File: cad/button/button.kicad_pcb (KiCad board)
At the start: 2 copper layers, 60 x 20 mm, 17 parts, among them J1 uSD_SPI, J2 SWD, SW1 SW_Push, U1 STM32L072KZTx, U2 PAM8302AAS

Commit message: more drawing
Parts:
- J1: footprint Connectors:microSD_Card_Receptacle_Wuerth_693072010801 -> custom:PJRC_uSD_Adapter; moved to B.Cu
- SW1: footprint Buttons_Switches_THT:SW_PUSH-12mm -> custom:SW_PUSH-12mm
- moved J2 57.4 mm to (52.8, 63.0), turned to 270 degrees
- moved BT1 47.5 mm to (29.0, 63.2), turned to 0 degrees
- moved R4 41.7 mm to (63.0, 46.0)
- moved LS1 39.4 mm to (66.9, 39.0), turned to 180 degrees
- moved U2 35.7 mm to (67.0, 46.0), turned to 90 degrees
- moved C2 33.0 mm to (27.0, 54.0), turned to 270 degrees
- moved C4 31.3 mm to (34.0, 58.0), turned to 0 degrees
- moved C1 30.7 mm to (27.0, 50.0), turned to 270 degrees
- moved U1 30.4 mm to (34.0, 51.0)
- moved SW1 30.2 mm to (46.5, 57.4)
- moved C5 27.1 mm to (27.0, 44.0), turned to 270 degrees
- moved R3 25.1 mm to (59.0, 55.0), turned to 180 degrees
- moved C6 24.8 mm to (59.0, 51.0), turned to 0 degrees
- moved R2 24.6 mm to (59.0, 53.0)
- moved R1 22.3 mm to (32.0, 43.0), turned to 90 degrees
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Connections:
- J1 pad 1: (no net) -> GND
- J1 pad 3: SD_MOSI -> SD_SCK
- J1 pad 4: +3V3 -> SD_MOSI
- J1 pad 5: SD_SCK -> SD_MISO
- J1 pad 6: GND -> (no net)
- J1 pad 7: SD_MISO -> (no net)
- J1 pad 9: Net-(J1-Pad9) -> (no net)
- U1 pad 18: SPK_SD -> Net-(U1-Pad18)
- U1 pad 25: Net-(U1-Pad25) -> SPK_SD
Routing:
- net Net-(J1-Pad9): track 37.2 -> 0.00 mm
- net SPK_IN: track 16.5 -> 40.2 mm
- net SD_MISO: track 53.1 -> 32.6 mm, vias 2 -> 1
- net SPK_SD: track 12.2 -> 30.1 mm, vias 0 -> 2
- net SD_SCK: track 51.3 -> 36.6 mm, vias 0 -> 1
- net SD_MOSI: track 46.7 -> 33.4 mm, vias 0 -> 1
- net /SWCLK: track 8.31 -> 21.1 mm
- net +3V3: track 14.3 -> 4.80 mm, vias 2 -> 0
- net /BOOT0: track 10.5 -> 2.65 mm, vias 2 -> 0
- net /SWDIO: track 11.4 -> 18.4 mm
- net SD_CS: track 44.5 -> 37.7 mm, vias 0 -> 1
- net /SPK_1: track 11.8 -> 5.01 mm, vias 1 -> 0
- net GND: track 30.8 -> 37.0 mm, vias 8 -> 5
- net /SPK_2: track 10.7 -> 5.09 mm, vias 1 -> 0
- net /SW_IN: track 34.2 -> 30.7 mm
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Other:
- board size 60 x 20 mm -> 58 x 44 mm
- board text added: "SWCK"
- board text added: "SWD"
- board text added: "SWIO"
- board text removed: "SWCLK"
- board text removed: "SWDIO"

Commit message: finish up schematic
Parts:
- added C10: 220pF, Capacitors_SMD:C_0603_HandSoldering, F.Cu at (62.0, 35.0)
- added C11: 220pF, Capacitors_SMD:C_0603_HandSoldering, F.Cu at (70.0, 35.0)
- added C7: 1uF, Capacitors_SMD:C_0603_HandSoldering, F.Cu at (74.0, 60.5)
- added C8: 1uF, Capacitors_SMD:C_0603_HandSoldering, F.Cu at (72.0, 60.5)
- added C9: 10uF, Capacitors_SMD:C_0603_HandSoldering, F.Cu at (70.0, 39.0)
- added FB1: Ferrite_Bead_Small, Resistors_SMD:R_0603_HandSoldering, F.Cu at (67.0, 37.0)
- added FB2: Ferrite_Bead_Small, Resistors_SMD:R_0603_HandSoldering, F.Cu at (65.0, 37.0)
- added Q1: DMC2038LVT, TO_SOT_Packages_SMD:TSOT-23-6, F.Cu at (29.5, 56.0)
- added R5: 10K, Resistors_SMD:R_0603_HandSoldering, F.Cu at (66.5, 45.0)
- added R6: 10K, Resistors_SMD:R_0603_HandSoldering, F.Cu at (75.0, 56.0)
- added R7: 10K, Resistors_SMD:R_0603_HandSoldering, F.Cu at (72.0, 52.5)
- added R8: 10K, Resistors_SMD:R_0603_HandSoldering, F.Cu at (72.0, 46.0)
- added REF**: MountingHole_0.5mm, custom:MountingHole_0.5mm, F.Cu at (72.5, 56.0)
- added REF**: MountingHole_1.5mm, custom:MountingHole_1.5mm, F.Cu at (74.5, 51.0)
- added REF**: MountingHole_3mm, Mounting_Holes:MountingHole_3mm, F.Cu at (59.0, 60.5)
- added REF**: MountingHole_3mm, Mounting_Holes:MountingHole_3mm, F.Cu at (39.0, 60.5)
- added REF**: MountingHole_3mm, Mounting_Holes:MountingHole_3mm, F.Cu at (59.0, 41.0)
- added REF**: MountingHole_3mm, Mounting_Holes:MountingHole_3mm, F.Cu at (39.0, 41.0)
- added REF**: MountingHole_1.5mm, custom:MountingHole_1.5mm, F.Cu at (23.5, 51.0)
- added REF**: MountingHole_0.5mm, custom:MountingHole_0.5mm, F.Cu at (25.5, 56.0)
- added RV1: R_POT, Potentiometers:Potentiometer_Trimmer-EVM3E, F.Cu at (68.0, 63.5)
- C1: value 100nF -> 10uF
- C2: value 1uF -> 10uF
- C3: value 10uF -> 100nF
- C5: value 100nF -> 1uF
- R2: value 1K -> 10K
- R3: value 10K -> not fitted
- R4: value 10K -> 10
- SW1: value SW_Push -> Button; footprint custom:SW_PUSH-12mm -> Buttons_Switches_THT:SW_PUSH-12mm
- moved C2 40.8 mm to (67.5, 59.0)
- moved C4 35.5 mm to (69.5, 59.0), turned to 90 degrees
- moved R2 34.5 mm to (24.5, 54.0)
- moved C3 33.0 mm to (62.0, 45.0), turned to 0 degrees
- moved U1 31.5 mm to (65.5, 51.0)
- moved C5 30.7 mm to (57.0, 50.5)
- moved R3 29.6 mm to (29.5, 52.5)
- moved R1 17.2 mm to (29.5, 60.0), turned to 180 degrees
- moved C1 9.34 mm to (24.5, 59.0), turned to 180 degrees
- moved LS1 6.07 mm to (66.0, 33.0)
- moved R4 6.02 mm to (59.0, 50.5)
- moved U2 4.47 mm to (69.0, 42.0), turned to 180 degrees
- moved C6 2.69 mm to (58.0, 53.5)
- moved BT1 0.25 mm to (29.0, 63.5)
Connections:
- BT1 pad 1: +3V3 -> /VBAT
- C1 pad 1: GND -> /VBAT
- C1 pad 2: +3V3 -> GND
- C3 pad 1: +3V3 -> GND
- C3 pad 2: GND -> +3V3
- C5 pad 2: +3V3 -> /VDDA
- C6 pad 1: /SW_IN -> GND
- C6 pad 2: +3V3 -> /VDDA
- LS1 pad 1: /SPK_1 -> /SPK+
- LS1 pad 2: /SPK_2 -> /SPK-
- R1 pad 1: /BOOT0 -> /GATE_N
- R1 pad 2: GND -> /VBAT
- R2 pad 1: Net-(R2-Pad1) -> /GATE_P
- R2 pad 2: /SW_IN -> GND
- R3 pad 1: Net-(R2-Pad1) -> +3V3
- R3 pad 2: GND -> /GATE_P
- R4 pad 1: GND -> +3V3
- R4 pad 2: SPK_SD -> /VDDA
- SW1 pad 1: Net-(R2-Pad1) -> /GATE_N
- SW1 pad 2: +3V3 -> GND
- U1 pad 10: SPK_IN -> SPK_IN+
- U1 pad 11: SD_SCK -> SPK_IN-
- U1 pad 12: SD_MISO -> Net-(U1-Pad12)
- U1 pad 13: SD_MOSI -> Net-(U1-Pad13)
- U1 pad 14: SD_CS -> Net-(U1-Pad14)
- U1 pad 22: Net-(U1-Pad22) -> SPK_SD
- U1 pad 25: SPK_SD -> SD_CS
- U1 pad 26: Net-(U1-Pad26) -> SD_SCK
- U1 pad 27: Net-(U1-Pad27) -> SD_MISO
- U1 pad 28: Net-(U1-Pad28) -> SD_MOSI
- U1 pad 5: +3V3 -> /VDDA
- U1 pad 6: /SW_IN -> Net-(U1-Pad6)
- U2 pad 3: SPK_IN -> Net-(R6-Pad1)
- U2 pad 4: GND -> Net-(R7-Pad1)
- U2 pad 5: /SPK_1 -> Net-(FB1-Pad1)
- U2 pad 8: /SPK_2 -> Net-(FB2-Pad1)
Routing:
- net +3V3: track 4.80 -> 126.3 mm
- net SPK_IN: track 40.2 -> 0.00 mm, vias 2 -> 0
- net GND: track 37.0 -> 3.95 mm, vias 5 -> 11
- net /SW_IN: track 30.7 -> 0.00 mm, vias 2 -> 0
- net /GATE_N: track 0.00 -> 24.7 mm, vias 0 -> 2
- net Net-(R6-Pad1): track 0.00 -> 21.4 mm
- net SPK_SD: track 30.1 -> 10.2 mm, vias 2 -> 0
- net Net-(R2-Pad1): track 18.8 -> 0.00 mm
- net SPK_IN-: track 0.00 -> 14.1 mm
- net Net-(R7-Pad1): track 0.00 -> 12.9 mm
- net SPK_IN+: track 0.00 -> 11.3 mm
- net /SWDIO: track 18.4 -> 29.7 mm
- net SD_MOSI: track 33.4 -> 22.1 mm
- net /VBAT: track 0.00 -> 10.6 mm
- net SD_CS: track 37.7 -> 27.2 mm
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- added copper zone on F.Cu, net GND
- removed copper zone on F.Cu, net +3V3
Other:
- outline, holes or cut-outs redrawn
- net class 3V3 removed
- net class Power added: clearance 0.2, trace_width 0.4, via_dia 0.9, via_drill 0.5

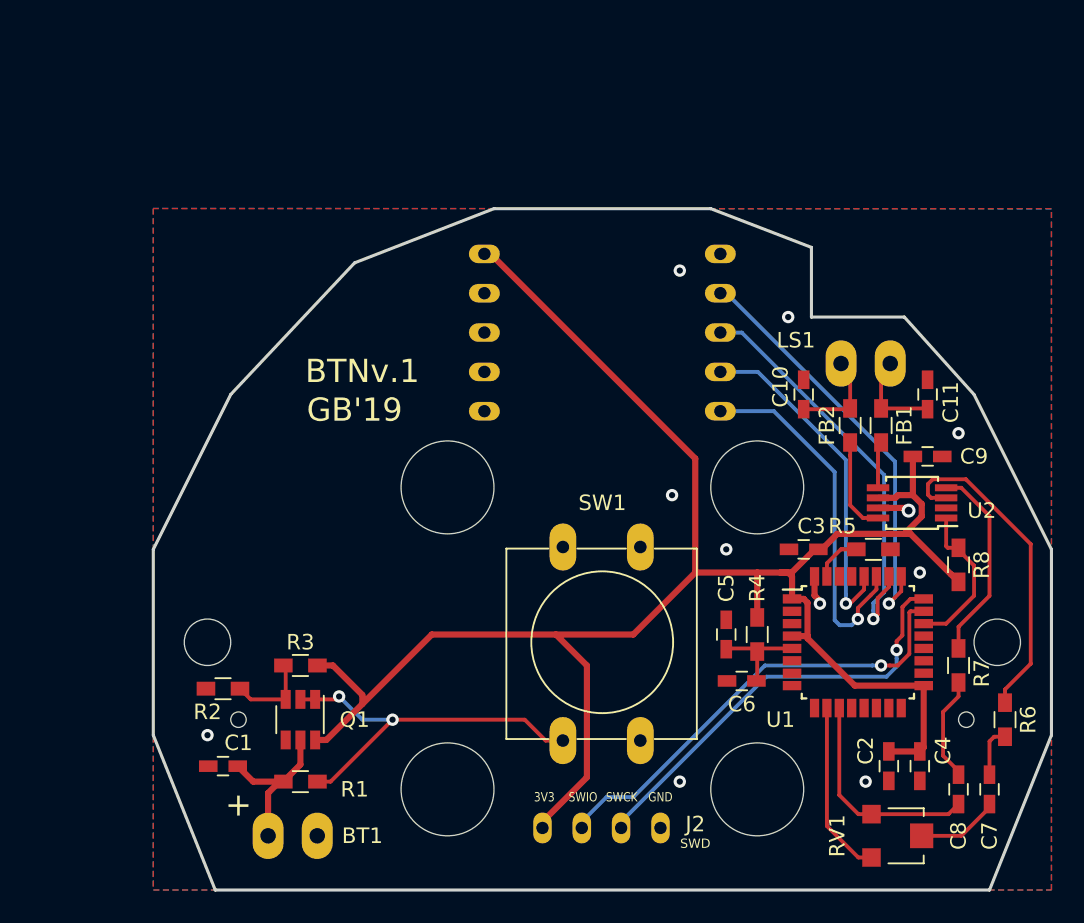
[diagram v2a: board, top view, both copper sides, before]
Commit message: move STM to below sdcard
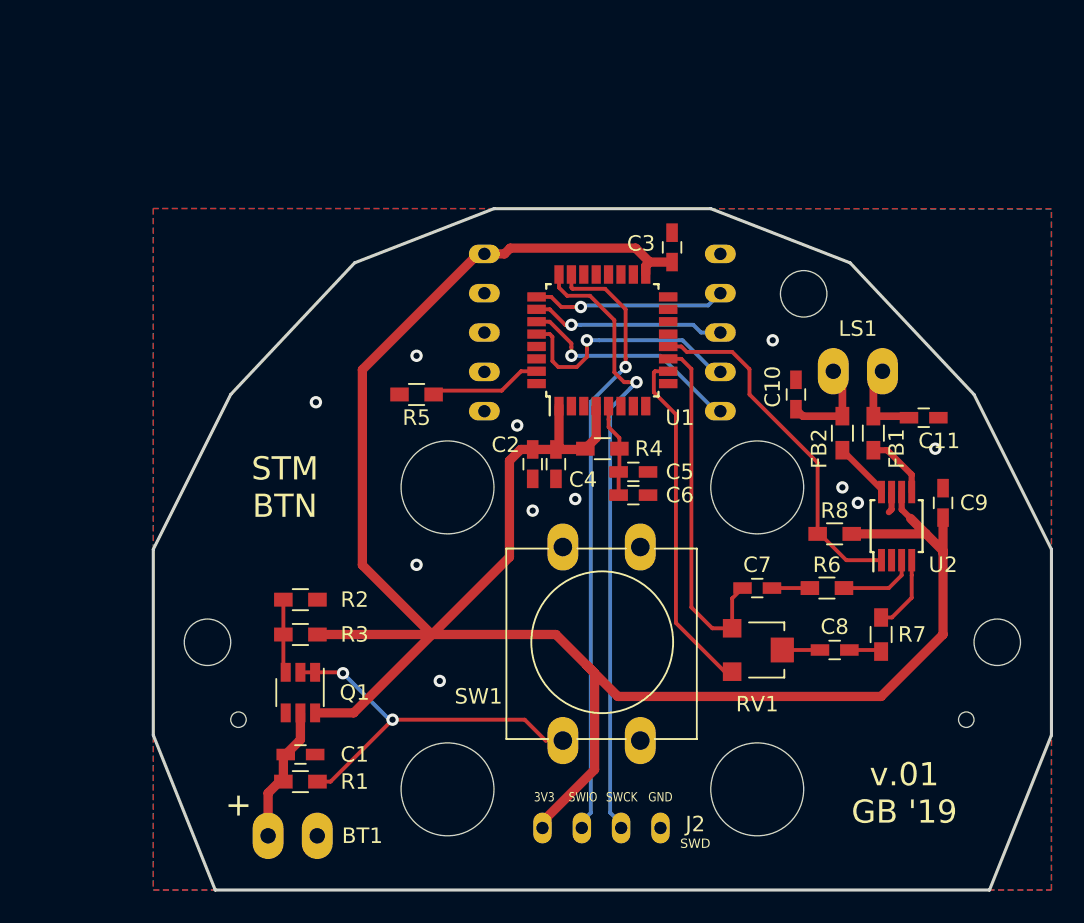
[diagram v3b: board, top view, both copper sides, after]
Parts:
- added REF**: MountingHole_1.5mm, custom:MountingHole_1.5mm, F.Cu at (62.0, 28.5)
- SW1: footprint Buttons_Switches_THT:SW_PUSH-12mm -> custom:SW_PUSH-12mm
- moved R5 31.1 mm to (37.0, 35.0), turned to 180 degrees
- moved C4 30.5 mm to (46.0, 39.5)
- moved C2 30.2 mm to (44.5, 39.5)
- moved U1 25.5 mm to (49.0, 31.5), turned to 90 degrees
- moved C3 21.3 mm to (53.5, 25.5), turned to 270 degrees
- moved C7 19.8 mm to (59.0, 47.5), turned to 180 degrees
- moved R4 15.6 mm to (49.0, 38.5), turned to 0 degrees
- moved RV1 15.0 mm to (59.0, 51.5)
- moved R6 14.3 mm to (63.5, 47.5), turned to 180 degrees
- moved C6 13.9 mm to (51.0, 41.5), turned to 180 degrees
- moved C5 12.1 mm to (51.0, 40.0), turned to 180 degrees
- moved C8 12.0 mm to (64.0, 51.5), turned to 180 degrees
- moved R8 8.25 mm to (64.0, 44.0), turned to 180 degrees
- moved R2 7.62 mm to (29.5, 48.2), turned to 0 degrees
- moved R7 5.39 mm to (67.0, 50.5)
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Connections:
- C7 pad 2: Net-(C7-Pad2) -> SPK_IN+
- C8 pad 2: SPK_IN- -> Net-(C8-Pad2)
- RV1 pad 1: SPK_IN- -> SPK_IN+
- RV1 pad 2: Net-(C7-Pad2) -> Net-(C8-Pad2)
- RV1 pad 3: SPK_IN+ -> SPK_IN-
- U1 pad 10: SPK_IN+ -> SPK_IN-
- U1 pad 11: SPK_IN- -> SPK_IN+
- U1 pad 12: Net-(U1-Pad12) -> SPK_SD
- U1 pad 22: SPK_SD -> Net-(U1-Pad22)
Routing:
- net +3V3: track 126.3 -> 150.6 mm
- net Net-(R6-Pad1): track 21.4 -> 5.04 mm
- net SD_CS: track 27.2 -> 12.5 mm
- net SD_SCK: track 27.1 -> 12.5 mm
- net SPK_SD: track 10.2 -> 23.1 mm
- net /SWCLK: track 27.9 -> 40.1 mm
- net SPK_IN+: track 11.3 -> 23.2 mm
- net /SWDIO: track 29.7 -> 39.6 mm
- net SD_MISO: track 23.6 -> 14.7 mm
- net SPK_IN-: track 14.1 -> 22.7 mm
- net Net-(R7-Pad1): track 12.9 -> 4.93 mm
- net SD_MOSI: track 22.1 -> 15.9 mm
- net Net-(C7-Pad2): track 5.36 -> 0.00 mm
- net Net-(C8-Pad1): track 6.78 -> 2.09 mm
- net /BOOT0: track 3.12 -> 7.27 mm
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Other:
- outline, holes or cut-outs redrawn
- net class Power: trace_width 0.4 -> 0.6
- net class SpkOut added: clearance 0.2, trace_width 0.4, via_dia 0.8, via_drill 0.4
- board text added: "STM BTN"
- board text added: "v.01 GB '19"
- board text removed: "BTNv.1"
- board text removed: "GB'19"

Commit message: update with help from Enno
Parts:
- added R9: 10K, Resistors_SMD:R_0603_HandSoldering, F.Cu at (64.0, 43.5)
- R6: value 10K -> 1K
- moved R6 34.0 mm to (29.5, 46.5), turned to 0 degrees
- moved J2 7.62 mm to (45.1, 63.0), turned to 90 degrees
- moved C1 5.93 mm to (31.5, 52.7)
- moved R8 5.81 mm to (66.5, 49.2)
- moved C9 5.70 mm to (65.5, 43.5)
- moved C7 3.76 mm to (62.8, 47.8)
- moved R7 2.80 mm to (66.5, 47.8), turned to 180 degrees
- moved C8 2.57 mm to (62.8, 49.2)
- moved Q1 2.08 mm to (31.2, 55.4), turned to 0 degrees
- moved RV1 2.06 mm to (58.5, 49.5), turned to 180 degrees
- moved R1 2.02 mm to (30.5, 58.2)
- moved U2 0.75 mm to (68.8, 43.5)
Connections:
- Q1 pad 1: /GATE_N -> POWERON
- Q1 pad 2: /GATE_N -> /VBAT
- Q1 pad 3: /GATE_P -> Net-(Q1-Pad3)
- Q1 pad 4: GND -> +3V3
- Q1 pad 5: /VBAT -> GND
- Q1 pad 6: +3V3 -> Net-(Q1-Pad3)
- R1 pad 1: /GATE_N -> Net-(Q1-Pad3)
- R2 pad 1: /GATE_P -> POWERON
- R3 pad 2: /GATE_P -> POWERON
- R6 pad 1: Net-(R6-Pad1) -> POWERON
- R6 pad 2: Net-(C7-Pad1) -> Net-(R6-Pad2)
- R7 pad 2: Net-(C8-Pad1) -> Net-(C7-Pad1)
- R8 pad 1: +3V3 -> Net-(R8-Pad1)
- R8 pad 2: SPK_SD -> Net-(C8-Pad1)
- SW1 pad 1: /GATE_N -> /VBAT
- SW1 pad 2: GND -> POWERON
- U1 pad 6: Net-(U1-Pad6) -> Net-(R6-Pad2)
- U2 pad 3: Net-(R6-Pad1) -> Net-(R7-Pad1)
- U2 pad 4: Net-(R7-Pad1) -> Net-(R8-Pad1)
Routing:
- net POWERON: track 0.00 -> 33.3 mm, vias 0 -> 2
- net Net-(R6-Pad2): track 0.00 -> 31.2 mm, vias 0 -> 2
- net /VBAT: track 8.95 -> 34.6 mm
- net /GATE_N: track 25.3 -> 0.00 mm, vias 2 -> 0
- net +3V3: track 150.6 -> 144.2 mm
- net Net-(Q1-Pad3): track 0.00 -> 6.31 mm
- net Net-(R6-Pad1): track 5.04 -> 0.00 mm
- net SPK_SD: track 23.1 -> 28.2 mm
- net /GATE_P: track 4.75 -> 0.00 mm
- net SPK_IN-: track 22.7 -> 18.1 mm
- net Net-(R8-Pad1): track 0.00 -> 4.41 mm
- net GND: track 1.37 -> 4.47 mm, vias 11 -> 26
- net /SWCLK: track 40.1 -> 37.1 mm
- net SD_MOSI: track 15.9 -> 12.9 mm
- net Net-(R7-Pad1): track 4.93 -> 2.65 mm
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
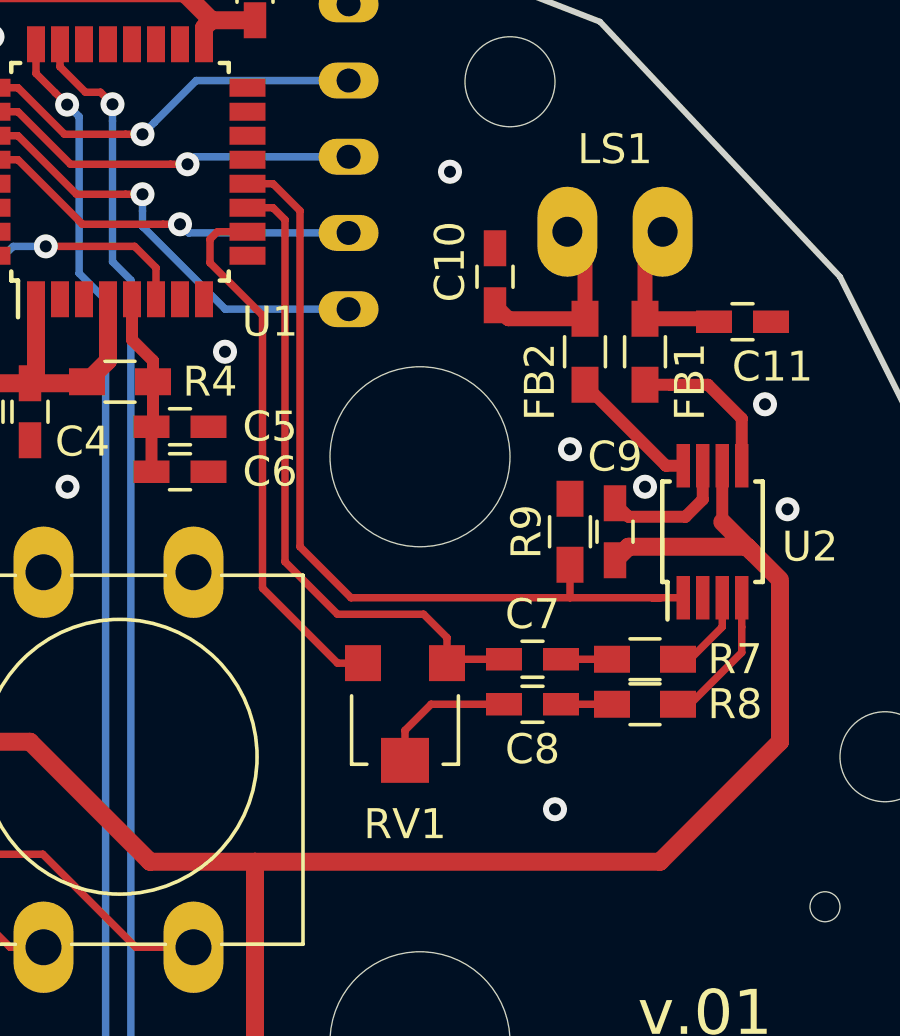
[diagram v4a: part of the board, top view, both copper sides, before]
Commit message: update Pot footprint
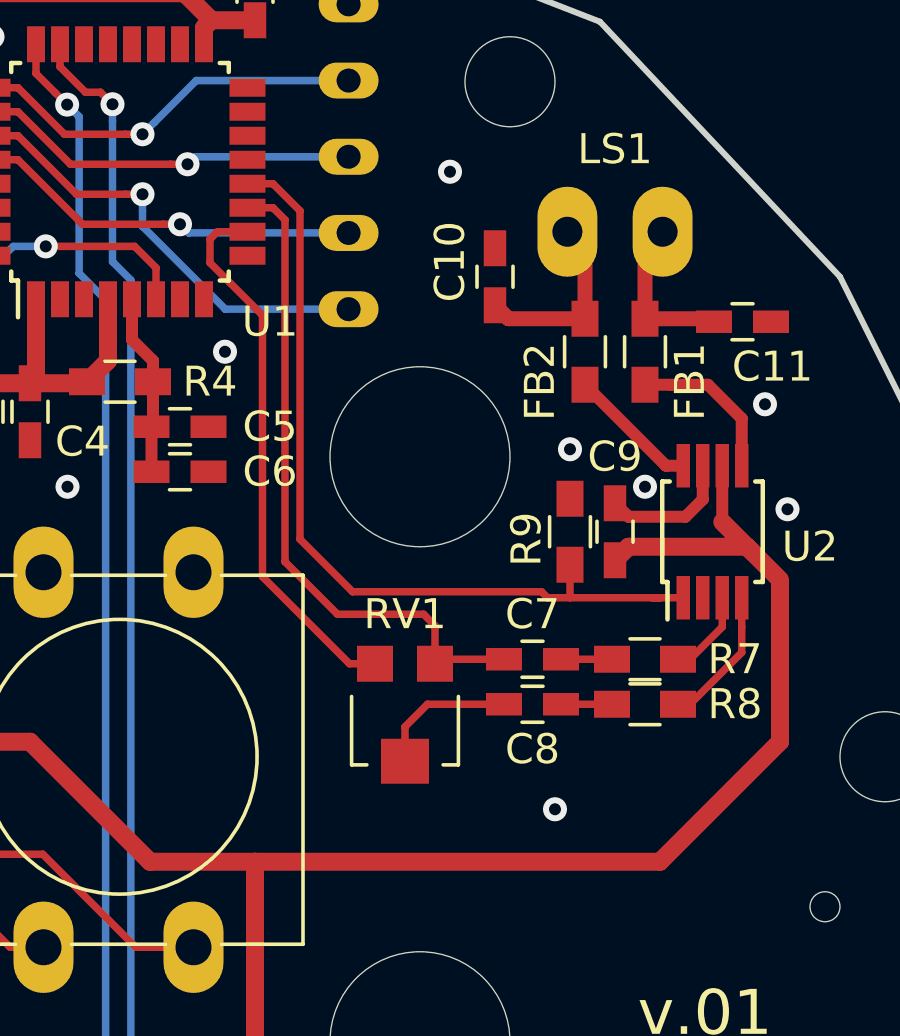
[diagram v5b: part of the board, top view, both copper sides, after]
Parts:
- RV1: value R_POT -> 10k; footprint Potentiometers:Potentiometer_Trimmer-EVM3E -> custom:Potentiometer_Trimmer-EVM3Y
